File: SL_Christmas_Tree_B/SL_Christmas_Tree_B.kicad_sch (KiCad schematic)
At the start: 60 parts, among them J101 5V, J102 5V, J201 GND, J202 GND

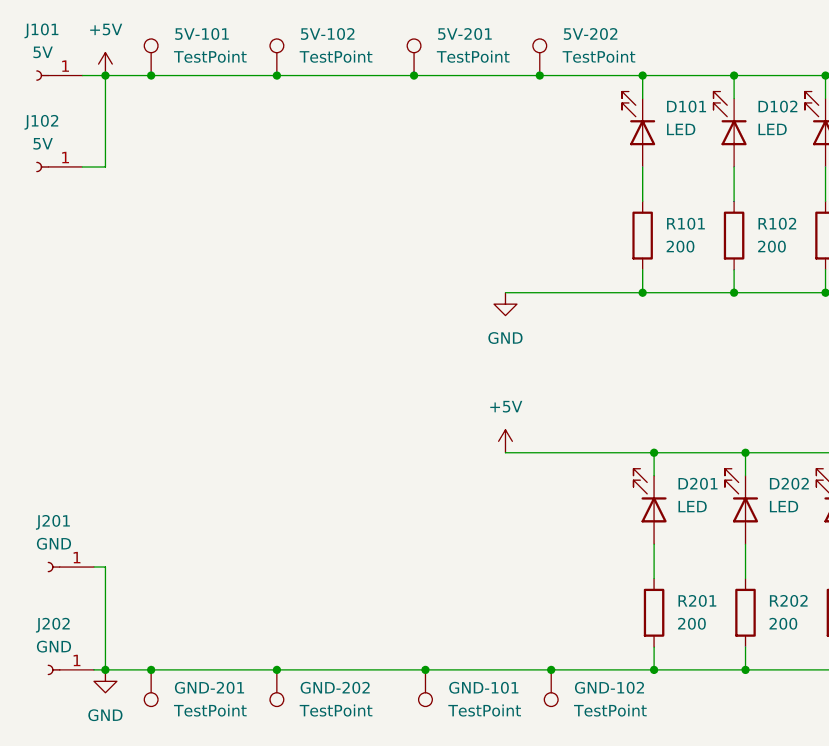
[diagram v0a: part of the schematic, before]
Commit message: fix swapped 5V / GND
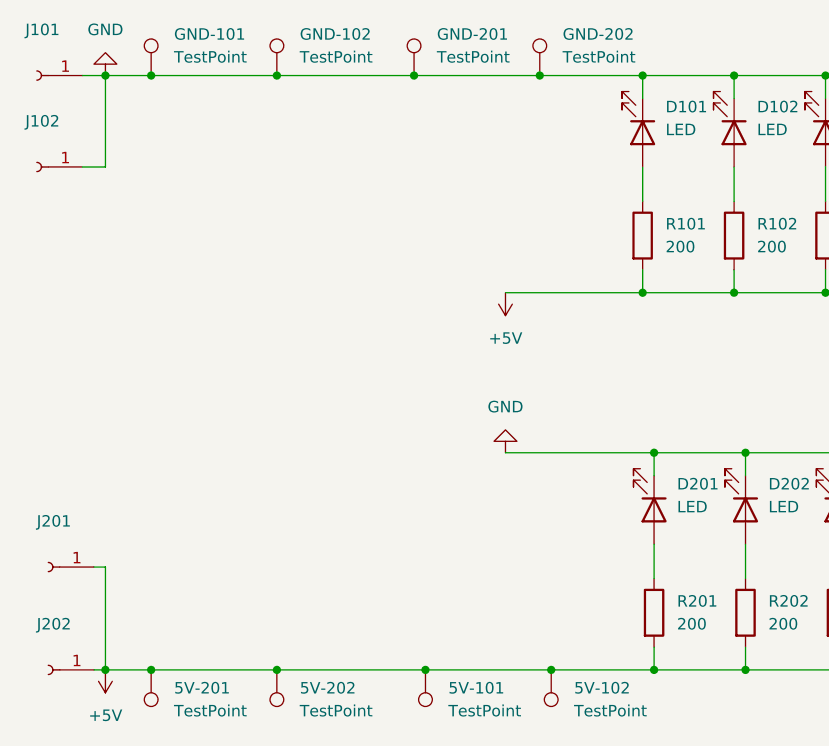
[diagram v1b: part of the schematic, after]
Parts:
- J101, J102: value 5V -> (none); footprint (none) -> TestPoint:TestPoint_Pad_3.0x3.0mm
- J201, J202: value GND -> (none); footprint (none) -> TestPoint:TestPoint_Pad_3.0x3.0mm
- renumbered GND-101 to 5V-101, GND-102 to 5V-102, GND-201 to 5V-201, GND-202 to 5V-202, 5V-101 to GND-101, 5V-102 to GND-102, 5V-201 to GND-201, 5V-202 to GND-202
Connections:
- net +5V: now also 5V-101.1, 5V-102.1, 5V-201.1, 5V-202.1, J201.1 (Pin_1), J202.1 (Pin_1), R101.2, R102.2, R103.2, R104.2, R105.2, R106.2, R107.2, R108.2, R109.2, R110.2, R111.2, R112.2, R201.2, R202.2, R203.2, R204.2, R205.2, R206.2, R207.2, R208.2, R209.2, R210.2, R211.2, R212.2; no longer D101.1 (K), D102.1 (K), D103.1 (K), D104.1 (K), D105.1 (K), D106.1 (K), D107.1 (K), D108.1 (K), D109.1 (K), D110.1 (K), D111.1 (K), D112.1 (K), D201.1 (K), D202.1 (K), D203.1 (K), D204.1 (K), D205.1 (K), D206.1 (K), D207.1 (K), D208.1 (K), D209.1 (K), D210.1 (K), D211.1 (K), D212.1 (K), GND-101.1, GND-102.1, GND-201.1, GND-202.1, J101.1 (Pin_1), J102.1 (Pin_1)
- net GND: now also D101.1 (K), D102.1 (K), D103.1 (K), D104.1 (K), D105.1 (K), D106.1 (K), D107.1 (K), D108.1 (K), D109.1 (K), D110.1 (K), D111.1 (K), D112.1 (K), D201.1 (K), D202.1 (K), D203.1 (K), D204.1 (K), D205.1 (K), D206.1 (K), D207.1 (K), D208.1 (K), D209.1 (K), D210.1 (K), D211.1 (K), D212.1 (K), GND-101.1, GND-102.1, GND-201.1, GND-202.1, J101.1 (Pin_1), J102.1 (Pin_1); no longer 5V-101.1, 5V-102.1, 5V-201.1, 5V-202.1, J201.1 (Pin_1), J202.1 (Pin_1), R101.2, R102.2, R103.2, R104.2, R105.2, R106.2, R107.2, R108.2, R109.2, R110.2, R111.2, R112.2, R201.2, R202.2, R203.2, R204.2, R205.2, R206.2, R207.2, R208.2, R209.2, R210.2, R211.2, R212.2

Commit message: small Footprint changes and prepared "Side B" for placing parts
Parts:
- removed D101, D102, D103, D104, D105, D106, D107, D108, D109, D110, D111, D112, D201, D202, D203, D204, D205, D206, D207, D208, D209, D210, D211, D212: LED, LED_SMD:LED_0807_Slow_Flashing_Diode, symbol Device:LED
- removed J101, J102, J201, J202: (no value), TestPoint:TestPoint_Pad_3.0x3.0mm, symbol Connector:Conn_01x01_Female
- removed R101, R102, R103, R104, R105, R106, R107, R108, R109, R110, R111, R112, R201, R202, R203, R204, R205, R206, R207, R208, R209, R210, R211, R212: 200, Resistor_SMD:R_0805_2012Metric_Pad1.20x1.40mm_HandSolder, symbol Device:R
- added C101, C102, C103, C104, C105, C106, C107, C108, C109, C110, C111, C112, C113, C201, C202, C203, C204, C205, C206, C207, C208, C209, C210, C211, C212, C213: 100nF, Capacitor_SMD:C_0805_2012Metric_Pad1.18x1.45mm_HandSolder, symbol Device:C
- added D101, D102, D103, D104, D105, D106, D108, D109, D110, D111, D112, D113, D201, D202, D203, D204, D205, D206, D208, D209, D210, D211, D212, D213: SK6812MINI, parts:LED_SK6812MINI_PLCC4_3.5x3.5mm_P1.75mm, symbol LED:SK6812MINI
- added D107, D207: SK6812 4020, parts:LED_SK6812_4020, symbol LED_SK6812_4020:SK6812_4020
- added DIN101, DIN102, DIN201, DOUT101, DOUT201: TestPoint, TestPoint:TestPoint_Pad_3.0x3.0mm, symbol Connector:TestPoint
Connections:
- net +5V: now also C101.2, C102.2, C103.2, C104.2, C105.2, C106.2, C107.1, C108.2, C109.2, C110.2, C111.2, C112.2, C113.2, C201.2, C202.2, C203.2, C204.2, C205.2, C206.2, C207.1, C208.2, C209.2, C210.2, C211.2, C212.2, C213.2, D101.4 (VDD), D102.4 (VDD), D103.4 (VDD), D104.4 (VDD), D105.4 (VDD), D106.4 (VDD), D107.2 (VDD), D108.4 (VDD), D109.4 (VDD), D110.4 (VDD), D111.4 (VDD), D112.4 (VDD), D113.4 (VDD), D201.4 (VDD), D202.4 (VDD), D203.4 (VDD), D204.4 (VDD), D205.4 (VDD), D206.4 (VDD), D207.2 (VDD), D208.4 (VDD), D209.4 (VDD), D210.4 (VDD), D211.4 (VDD), D212.4 (VDD), D213.4 (VDD)
- net GND: now also C101.1, C102.1, C103.1, C104.1, C105.1, C106.1, C107.2, C108.1, C109.1, C110.1, C111.1, C112.1, C113.1, C201.1, C202.1, C203.1, C204.1, C205.1, C206.1, C207.2, C208.1, C209.1, C210.1, C211.1, C212.1, C213.1, D101.2 (VSS), D102.2 (VSS), D103.2 (VSS), D104.2 (VSS), D105.2 (VSS), D106.2 (VSS), D107.4 (GND), D108.2 (VSS), D109.2 (VSS), D110.2 (VSS), D111.2 (VSS), D112.2 (VSS), D113.2 (VSS), D201.2 (VSS), D202.2 (VSS), D203.2 (VSS), D204.2 (VSS), D205.2 (VSS), D206.2 (VSS), D207.4 (GND), D208.2 (VSS), D209.2 (VSS), D210.2 (VSS), D211.2 (VSS), D212.2 (VSS), D213.2 (VSS)
- new net: D109.1 (DOUT), D110.3 (DIN)
- new net: D108.1 (DOUT), D109.3 (DIN)
- new net: D205.1 (DOUT), D206.3 (DIN)
- new net: D204.1 (DOUT), D205.3 (DIN)
- new net: D206.1 (DOUT), D207.1 (DIN)
- new net: D105.1 (DOUT), D106.3 (DIN)
- new net: D104.1 (DOUT), D105.3 (DIN)
- new net: D103.1 (DOUT), D104.3 (DIN)
- new net: D106.1 (DOUT), D107.1 (DIN)
- new net: D107.3 (DOUT), DOUT101.1
- new net: D112.1 (DOUT), D113.3 (DIN)
- new net: D111.1 (DOUT), D112.3 (DIN)
- new net: D208.1 (DOUT), D209.3 (DIN)
- new net: D208.3 (DIN), DIN201.1
- new net: D101.1 (DOUT), D102.3 (DIN)
- new net: D101.3 (DIN), DIN101.1
- new net: D207.3 (DOUT), DOUT201.1
- new net: D211.1 (DOUT), D212.3 (DIN)
- new net: D210.1 (DOUT), D211.3 (DIN)
- new net: D110.1 (DOUT), D111.3 (DIN)
- new net: D209.1 (DOUT), D210.3 (DIN)
- new net: D108.3 (DIN), DIN102.1
- new net: D203.1 (DOUT), D204.3 (DIN)
- new net: D212.1 (DOUT), D213.3 (DIN)
- new net: D102.1 (DOUT), D103.3 (DIN)
- new net: D202.1 (DOUT), D203.3 (DIN)
- new net: D201.1 (DOUT), D202.3 (DIN)
- new net Conn_A-OUT_B-IN: D113.1 (DOUT), D201.3 (DIN)
- no-connect marks 0 -> 1
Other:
- note added: "Side A"
- note added: "Side B"
- company: (none) -> Sternenlabor e.V.
- title: (none) -> Christmas Tree 2024 - Side B

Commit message: WIP v2.1
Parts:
- removed C107, C207: 100nF, Capacitor_SMD:C_0805_2012Metric_Pad1.18x1.45mm_HandSolder, symbol Device:C
- removed D107, D207: SK6812 4020, parts:LED_SK6812_4020, symbol LED_SK6812_4020:SK6812_4020
- removed DIN102: TestPoint, TestPoint:TestPoint_Pad_3.0x3.0mm, symbol Connector:TestPoint
- added 5V-103, 5V-203, GND-103, GND-203: TestPoint, TestPoint:TestPoint_Pad_3.0x3.0mm, symbol Connector:TestPoint
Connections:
- net +5V: now also 5V-103.1, 5V-203.1
- net Conn_A-OUT_B-IN: now also D106.1 (DOUT); no longer D113.1 (DOUT)
- net GND: now also GND-103.1, GND-203.1
- net at D206.1 (DOUT): now also DOUT201.1
- net at DOUT101.1: now also D113.1 (DOUT)
- net Conn_B-OUT_A-IN: now reaches D108.3 (DIN)
- net Conn_B-OUT_A-IN: now also D213.1 (DOUT)
- no-connect marks 1 -> 0
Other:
- moved on the sheet: 5V-101, 5V-102, 5V-201, 5V-202, DIN101, DOUT201, GND-101, GND-102, GND-201, GND-202
